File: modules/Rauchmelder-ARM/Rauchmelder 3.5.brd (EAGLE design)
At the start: 38 x 65 mm, 61 parts, among them IC2 LPC1115, IC3 BD9G101, Q1 BC856, Q3 BCP52, Q4 ASFL, T1 BC848

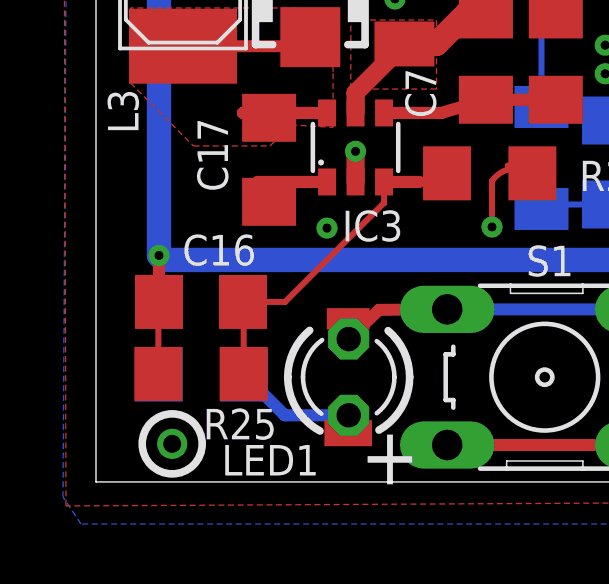
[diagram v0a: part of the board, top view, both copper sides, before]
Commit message: Unrouted error behoben
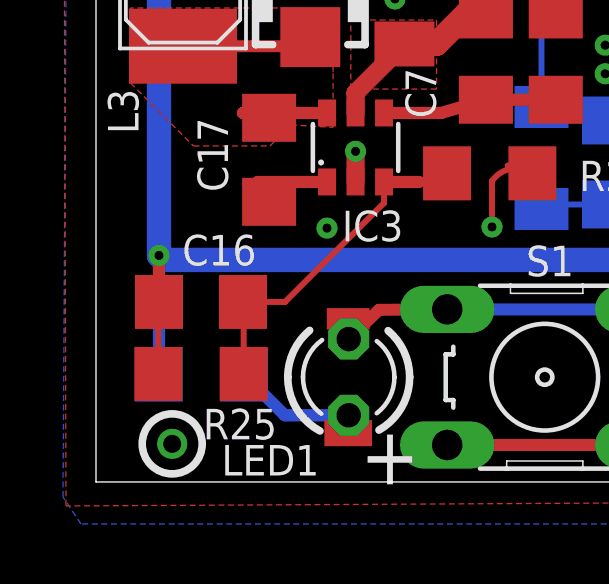
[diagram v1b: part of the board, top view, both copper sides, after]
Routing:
- net VCC: track 141.8 -> 145.8 mm
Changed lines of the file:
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@@
 <grid distance="3.125" unitdist="mil" unit="mil" style="lines" multiple="1" display="yes" altdistance="6.25" altunitdist="mil" altunit="mil"/>
 <layers>
-<layer number="1" name="Top" color="4" fill="1" visible="yes" active="yes"/>
+<layer number="1" name="Top" color="4" fill="1" visible="no" active="yes"/>
 <layer number="2" name="Route2" color="1" fill="3" visible="no" active="no"/>
 <layer number="3" name="Route3" color="4" fill="3" visible="no" active="no"/>
@@
 <layer number="14" name="Route14" color="1" fill="6" visible="no" active="no"/>
 <layer number="15" name="Route15" color="4" fill="6" visible="no" active="no"/>
-<layer number="16" name="Bottom" color="1" fill="1" visible="no" active="yes"/>
+<layer number="16" name="Bottom" color="1" fill="1" visible="yes" active="yes"/>
 <layer number="17" name="Pads" color="2" fill="1" visible="yes" active="yes"/>
 <layer number="18" name="Vias" color="2" fill="1" visible="yes" active="yes"/>
@@
 <layer number="21" name="tPlace" color="7" fill="1" visible="yes" active="yes"/>
 <layer number="22" name="bPlace" color="7" fill="1" visible="no" active="yes"/>
-<layer number="23" name="tOrigins" color="15" fill="1" visible="yes" active="yes"/>
-<layer number="24" name="bOrigins" color="15" fill="1" visible="no" active="yes"/>
-<layer number="25" name="tNames" color="7" fill="1" visible="yes" active="yes"/>
+<layer number="23" name="tOrigins" color="15" fill="1" visible="no" active="yes"/>
+<layer number="24" name="bOrigins" color="15" fill="1" visible="yes" active="yes"/>
+<layer number="25" name="tNames" color="7" fill="1" visible="no" active="yes"/>
 <layer number="26" name="bNames" color="7" fill="1" visible="no" active="yes"/>
 <layer number="27" name="tValues" color="7" fill="1" visible="no" active="yes"/>
 <layer number="28" name="bValues" color="7" fill="1" visible="no" active="yes"/>
-<layer number="29" name="tStop" color="7" fill="3" visible="yes" active="yes"/>
-<layer number="30" name="bStop" color="7" fill="6" visible="no" active="yes"/>
+<layer number="29" name="tStop" color="7" fill="3" visible="no" active="yes"/>
+<layer number="30" name="bStop" color="7" fill="6" visible="yes" active="yes"/>
 <layer number="31" name="tCream" color="7" fill="4" visible="no" active="yes"/>
 <layer number="32" name="bCream" color="7" fill="5" visible="no" active="yes"/>
@@
 <wire x1="35.45" y1="13.45" x2="35.472" y2="13.45" width="0.4064" layer="1"/>
 <wire x1="35.95" y1="13.928" x2="35.95" y2="19.4" width="0.4064" layer="1"/>
-<wire x1="2.078" y1="3.6" x2="2.09175" y2="3.58075" width="0" layer="19" extent="1-16"/>
+<wire x1="2.09175" y1="3.58075" x2="2.1" y2="3.58075" width="0.4064" layer="16"/>
+<wire x1="2.1" y1="3.58075" x2="2.1" y2="7.55" width="0.4064" layer="16"/>
 </signal>
 <signal name="N$2">

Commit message: Fix a few part values in Rauchmelder_3.5
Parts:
- C15: value 10µ/10V -> 22µ/10V
- C20: value (none) -> 100n
- C8: value 100n -> 10n
- R15: value 5k6 -> 100k
- T1: value BC848 -> BC847C
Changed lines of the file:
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@@
 <attribute name="VALUE" x="4.01885" y="53.219975" size="1.27" layer="27"/>
 </element>
-<element name="C8" library="rcl" package="C1206" value="100n" x="32.554475" y="11.073125" smashed="yes" rot="R180">
+<element name="C8" library="rcl" package="C1206" value="10n" x="32.554475" y="11.073125" smashed="yes" rot="R180">
 <attribute name="NAME" x="30.2245" y="11.46235" size="1.016" layer="25" ratio="10" rot="R180"/>
 <attribute name="VALUE" x="30.12625" y="11.230125" size="0.8128" layer="27" ratio="10" rot="R180"/>
 </element>
-<element name="R15" library="rcl" package="R1206" value="5k6" x="32.594475" y="8.747475" smashed="yes" rot="R180">
+<element name="R15" library="rcl" package="R1206" value="100k" x="32.594475" y="8.747475" smashed="yes" rot="R180">
 <attribute name="NAME" x="30.2296" y="9.4527" size="1.016" layer="25" ratio="10" rot="R180"/>
 <attribute name="VALUE" x="30.1152" y="9.850175" size="1.27" layer="27" ratio="10" rot="R180"/>
@@
 <attribute name="VALUE" x="12.931875" y="51.2675" size="1.27" layer="27" rot="R270"/>
 </element>
-<element name="T1" library="transistor" package="SOT23" value="BC848" x="15.825" y="27.7425" smashed="yes" rot="R90">
+<element name="T1" library="transistor" package="SOT23" value="BC847C" x="15.825" y="27.7425" smashed="yes" rot="R90">
 <attribute name="NAME" x="15.79625" y="26.8225" size="1.016" layer="25" rot="R180"/>
 <attribute name="VALUE" x="-1.19" y="27.779375" size="1.27" layer="27" rot="R180"/>
@@
 <attribute name="VALUE" x="12.387" y="12.549" size="1.27" layer="28" rot="MR90"/>
 </element>
-<element name="C20" library="rcl" package="C1206" value="" x="17.1" y="10.65" smashed="yes" rot="MR90">
+<element name="C20" library="rcl" package="C1206" value="100n" x="17.1" y="10.65" smashed="yes" rot="MR90">
 <attribute name="NAME" x="18.3575" y="9.540625" size="1.016" layer="26" rot="MR90"/>
 <attribute name="VALUE" x="14.56" y="9.38" size="1.27" layer="28" rot="MR90"/>
@@
 <attribute name="VALUE" x="-7.768125" y="18.35" size="1.016" layer="27"/>
 </element>
-<element name="C15" library="rcl" package="C1206" value="10µ/10V" x="5" y="21.4" smashed="yes" rot="R180">
+<element name="C15" library="rcl" package="C1206" value="22µ/10V" x="5" y="21.4" smashed="yes" rot="R180">
 <attribute name="NAME" x="2.9" y="21.279375" size="1.016" layer="25" rot="R180"/>
 <attribute name="VALUE" x="-0.45" y="22.05" size="1.016" layer="27" rot="R180"/>
